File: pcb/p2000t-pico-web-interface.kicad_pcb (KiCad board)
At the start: 2 copper layers, 80 x 100 mm, 23 parts, among them J1 P2000T Port 2, U1 74LVC273, U2 74HCT245, U3 74HCT245, U5 74LVC74, U6 74LVC08, U7 74HC32, U8 74HCT688, U9 74HCT138

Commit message: Removing diode from design, hardening interface
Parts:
- removed D1: 1N4148, Diode_THT:D_DO-35_SOD27_P7.62mm_Horizontal
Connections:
- A1 pad 30: Net-(A1-RUN) -> unconnected-(A1-RUN-Pad30)
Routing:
- net Net-(A1-RUN): track 41.4 -> 0.00 mm, vias 1 -> 0
- net ~{RES_3V3}: track 8.10 -> 0.00 mm
- net PD13: vias 5 -> 4
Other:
- board text added: "v1.1"

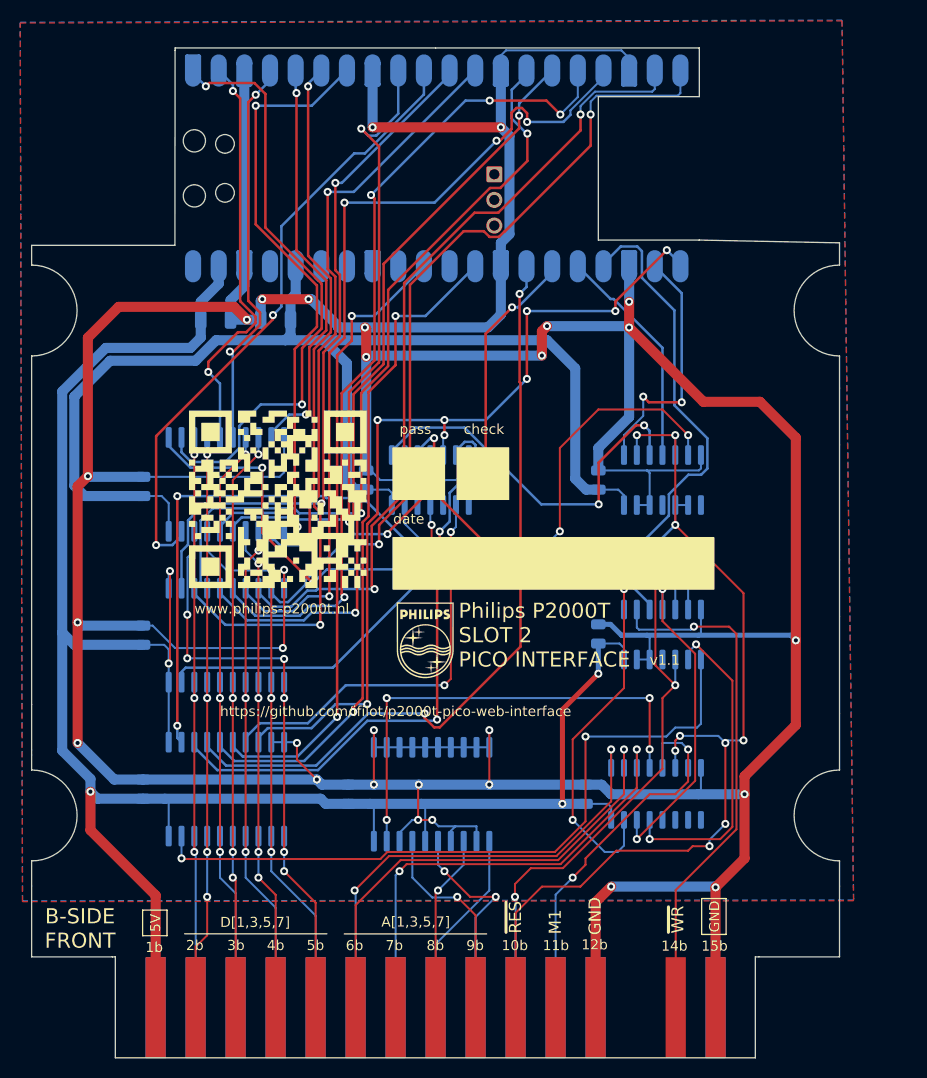
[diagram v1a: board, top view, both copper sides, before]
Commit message: Changing language to Dutch and adding new shortkeys (#1)
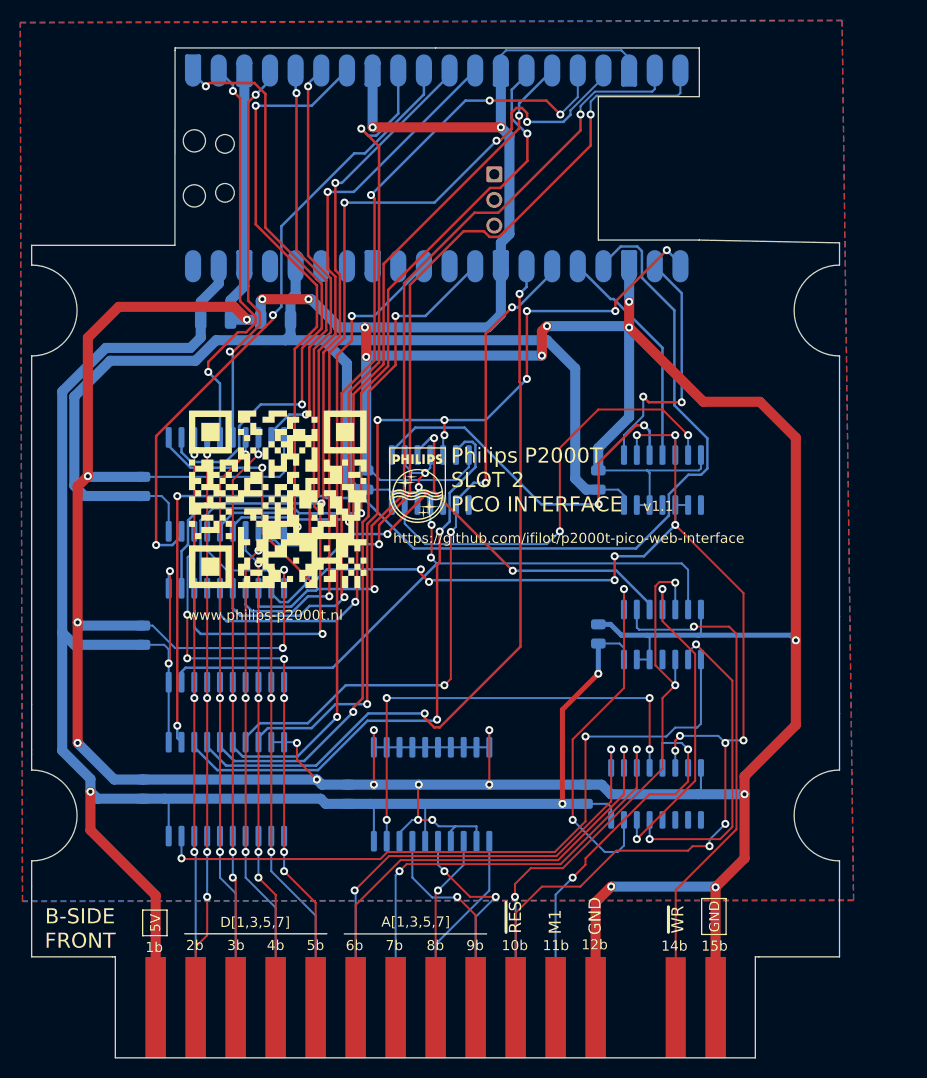
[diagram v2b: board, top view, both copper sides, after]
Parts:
- moved G003 15.4 mm to (59.8, 61.1)
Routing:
- net PD9: track 78.2 -> 81.8 mm
- net PD12: track 82.9 -> 83.8 mm
- net PD14: track 81.0 -> 81.8 mm
- net PD13: track 84.0 -> 84.7 mm
- net PD11: track 77.4 -> 78.1 mm
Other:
- board text removed: "check"
- board text removed: "date"
- board text removed: "pass"

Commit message: Adding LEDs to PCB
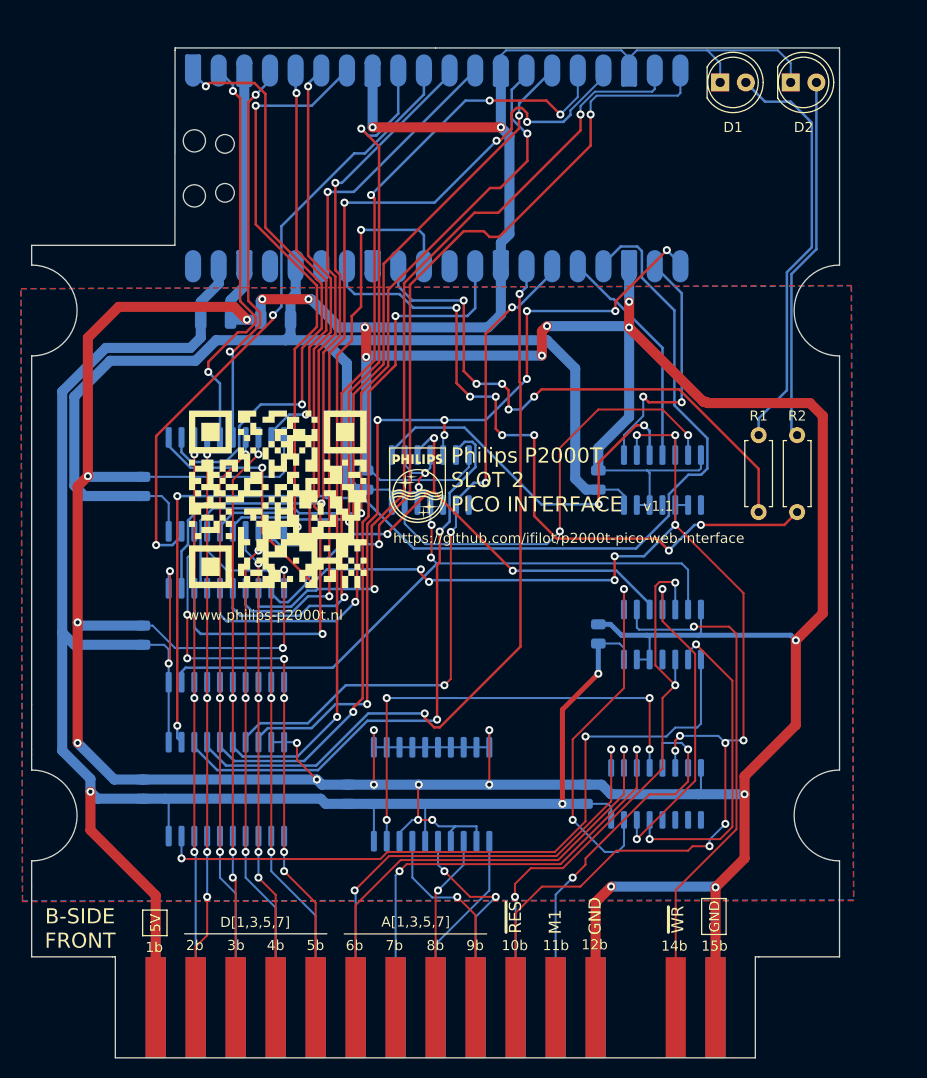
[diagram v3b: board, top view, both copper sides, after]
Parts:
- added D1: LED1, LED_THT:LED_D5.0mm, F.Cu at (89.8, 21.2)
- added D2: LED2, LED_THT:LED_D5.0mm, F.Cu at (96.8, 21.2)
- added R1: 1k, Resistor_THT:R_Axial_DIN0207_L6.3mm_D2.5mm_P7.62mm_Horizontal, F.Cu at (93.6, 63.7)
- added R2: 1k, Resistor_THT:R_Axial_DIN0207_L6.3mm_D2.5mm_P7.62mm_Horizontal, F.Cu at (97.4, 63.7)
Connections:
- A1 pad 32: unconnected-(A1-GPIO27_ADC1-Pad32) -> LED1
- A1 pad 34: unconnected-(A1-GPIO28_ADC2-Pad34) -> LED2
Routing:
- net LED2: track 0.00 -> 69.9 mm, vias 0 -> 7
- net LED1: track 0.00 -> 56.3 mm, vias 0 -> 5
- net Net-(D1-A): track 0.00 -> 41.3 mm
- net Net-(D2-A): track 0.00 -> 36.2 mm
- net GND: track 583.2 -> 610.7 mm
- net ERROR: track 62.3 -> 71.5 mm
- net BUSY: track 67.1 -> 69.6 mm
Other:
- outline, holes or cut-outs redrawn
